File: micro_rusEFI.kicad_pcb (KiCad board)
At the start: 4 copper layers, 80.6 x 93.7 mm, 180 parts, among them J1 USB_B_Micro, J19 Conn_01x06, J2 Conn_02x05_Odd_Even, J7 TC2030, SW1 SW_Push, SW2 SW_Push, SW3 SW_Push, SW4 SW_Push, U1 STM32F427VGT6, U2 LMR14020, U3 molex_48pin_MRE, U35 MCP6004, U36 MCP6004, U4 TJA1051T-3, U46 MCP6004, U5 LM1117-3.3, U6 TJA1051T-3, U8 MCP6004, X1 8MHz 20pF, Y2 32768 Hz

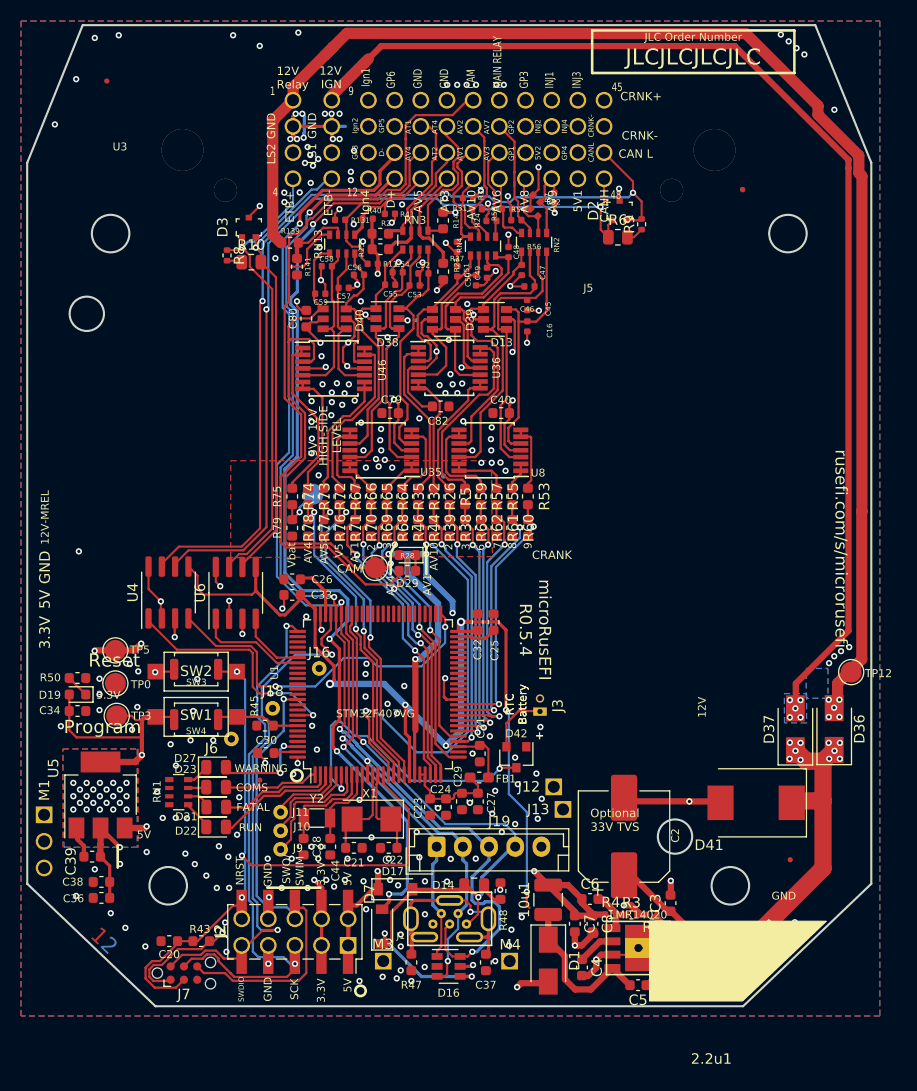
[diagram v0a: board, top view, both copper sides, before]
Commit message: Fixed CAN and 5v pads
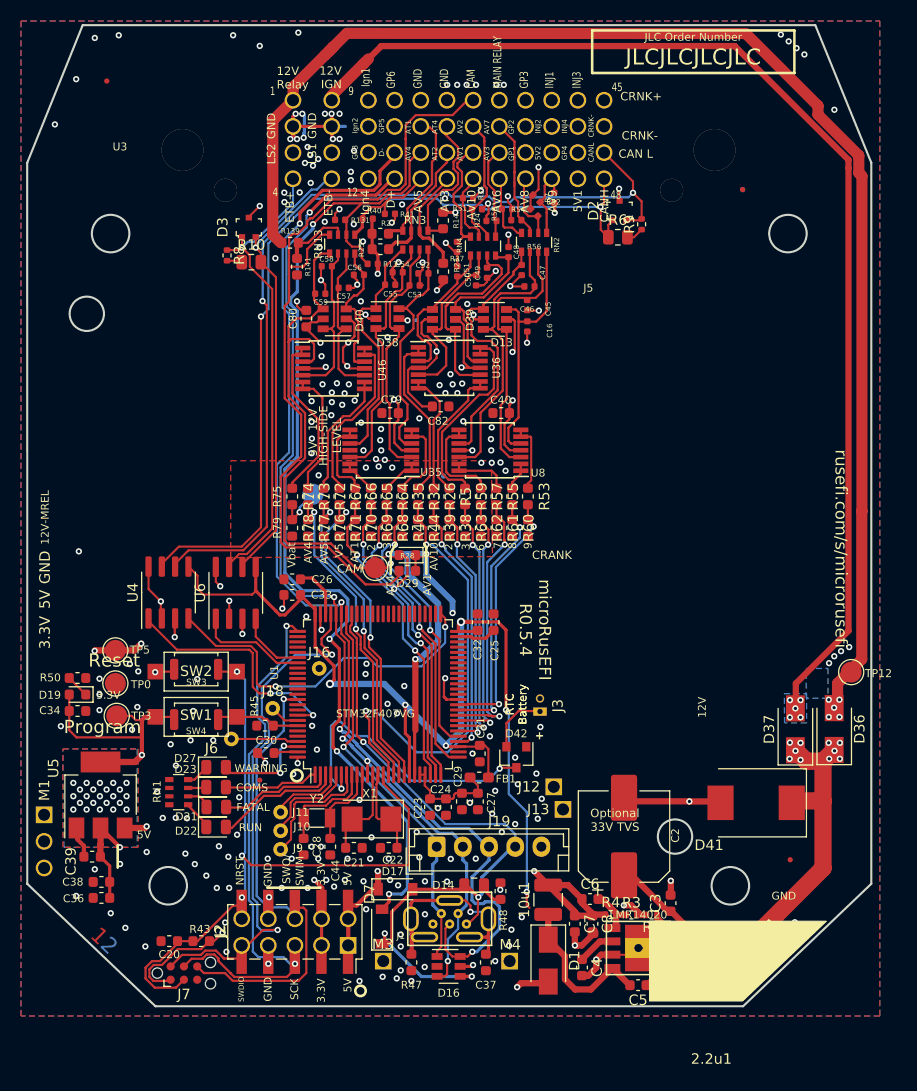
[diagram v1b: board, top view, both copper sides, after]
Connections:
- net /5V renamed 5V
- net /MCU/PB12 renamed /MCU/RXDCAN1
- net /VDD renamed VDD
- D2 pad 1: /CANH -> /CAN Transceiver/CANH1
- D2 pad 2: /CANL -> /CAN Transceiver/CANL1
- D3 pad 1: /CANL2 -> /CAN Transceiver/CANH2
- D3 pad 2: /CANH2 -> /CAN Transceiver/CANL2
- R10 pad 2: /CANH2 -> /CAN Transceiver/CANL2
- R6 pad 1: /CANH -> /CAN Transceiver/CANH1
- R8 pad 1: /CANL2 -> /CAN Transceiver/CANH2
- R9 pad 2: /CANL -> /CAN Transceiver/CANL1
- U3 pad 4: /CANL2 -> unconnected-(U3-Pad4)
- U3 pad 8: /CANH2 -> unconnected-(U3-Pad8)
- U4 pad 6: /CANH -> /CAN Transceiver/CANL1
- U4 pad 7: /CANL -> /CAN Transceiver/CANH1
- U6 pad 6: /CANH2 -> /CAN Transceiver/CANL2
- U6 pad 7: /CANL2 -> /CAN Transceiver/CANH2
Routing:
- net /CANL: track 85.8 -> 0.00 mm, vias 2 -> 0
- net /CAN Transceiver/CANL1: track 0.00 -> 85.1 mm, vias 0 -> 2
- net /CAN Transceiver/CANH1: track 0.00 -> 80.4 mm, vias 0 -> 2
- net /CANH: track 79.4 -> 0.00 mm, vias 2 -> 0
- net /CANL2: track 45.3 -> 0.00 mm, vias 1 -> 0
- net /CAN Transceiver/CANH2: track 0.00 -> 45.3 mm, vias 0 -> 1
- net /CANH2: track 43.8 -> 0.00 mm, vias 1 -> 0
- net /CAN Transceiver/CANL2: track 0.00 -> 43.8 mm, vias 0 -> 1
- net /MCU/PD1: track 0.00 -> 10.6 mm
- net /CAN Transceiver/TXDCAN2: track 10.6 -> 0.00 mm
- net /MCU/PD0: track 0.00 -> 6.53 mm
- net /CAN Transceiver/RXDCAN2: track 6.53 -> 0.00 mm
- net /PE0: track 0.00 -> 6.42 mm
- net /MCU/PB7: track 0.00 -> 2.86 mm

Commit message: Fixing tags
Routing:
- net /ADC/AGND: track 27.0 -> 37.3 mm
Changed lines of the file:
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@@
   (via (at 49.6824 57.4802) (size 0.6) (drill 0.3) (layers "F.Cu" "B.Cu") (net 1))
   (via (at 55 87.2) (size 0.6) (drill 0.3) (layers "F.Cu" "B.Cu") (net 1))
-  (via (at 79.216592 110.522348) (size 0.6) (drill 0.3) (layers "F.Cu" "B.Cu") (net 1))
+  (via (at 78.950449 110.517255) (size 0.6) (drill 0.3) (layers "F.Cu" "B.Cu") (net 1))
   (via (at 44.293286 44.657115) (size 0.6) (drill 0.3) (layers "F.Cu" "B.Cu") (net 1))
   (via (at 83.82 96.52) (size 0.6) (drill 0.3) (layers "F.Cu" "B.Cu") (free) (net 1))
@@
   (segment (start 52.697212 73.403792) (end 52.697212 71.965293) (width 0.2159) (layer "B.Cu") (net 70))
   (segment (start 56.977001 77.683581) (end 52.697212 73.403792) (width 0.2159) (layer "B.Cu") (net 70))
-  (segment (start 51.16464 72.064636) (end 52.100004 73) (width 0.2159) (layer "F.Cu") (net 71))
+  (segment (start 51.461883 72.3465) (end 51.16464 72.049257) (width 0.2159) (layer "F.Cu") (net 71))
   (segment (start 58.472361 92.455841) (end 58.472361 82.945397) (width 0.2159) (layer "F.Cu") (net 71))
   (segment (start 51.9 68.1875) (end 51.9 69.6125) (width 0.2159) (layer "F.Cu") (net 71))
-  (segment (start 51.16464 70.34786) (end 51.16464 72.064636) (width 0.2159) (layer "F.Cu") (net 71))
-  (segment (start 51.9 69.6125) (end 51.16464 70.34786) (width 0.2159) (layer "F.Cu") (net 71))
+  (segment (start 51.16464 72.049257) (end 51.16464 70.34786) (width 0.2159) (layer "F.Cu") (net 71))
   (segment (start 59.0868 93.9596) (end 59.0868 93.07028) (width 0.2159) (layer "F.Cu") (net 71))
   (segment (start 59.0868 93.07028) (end 58.472361 92.455841) (width 0.2159) (layer "F.Cu") (net 71))
+  (segment (start 51.16464 70.34786) (end 51.9 69.6125) (width 0.2159) (layer "F.Cu") (net 71))
   (segment (start 57.632561 82.105597) (end 58.472361 82.945397) (width 0.2159) (layer "F.Cu") (net 71))
   (via (at 57.632561 82.105597) (size 0.6) (drill 0.3) (layers "F.Cu" "B.Cu") (net 71))
-  (via (at 52.100004 73) (size 0.6) (drill 0.3) (layers "F.Cu" "B.Cu") (net 71))
-  (segment (start 52.100004 73.327454) (end 52.100004 73) (width 0.2159) (layer "B.Cu") (net 71))
-  (segment (start 56.462648 80.935684) (end 56.462648 77.690098) (width 0.2159) (layer "B.Cu") (net 71))
-  (segment (start 56.462648 77.690098) (end 52.100004 73.327454) (width 0.2159) (layer "B.Cu") (net 71))
-  (segment (start 57.632561 82.105597) (end 56.462648 80.935684) (width 0.2159) (layer "B.Cu") (net 71))
+  (via (at 51.461883 72.3465) (size 0.6) (drill 0.3) (layers "F.Cu" "B.Cu") (net 71))
+  (segment (start 51.461883 72.689333) (end 56.462648 77.690098) (width 0.2159) (layer "B.Cu") (net 71))
+  (segment (start 51.461883 72.3465) (end 51.461883 72.689333) (width 0.2159) (layer "B.Cu") (net 71))
+  (segment (start 56.462648 77.690098) (end 56.462648 80.935684) (width 0.2159) (layer "B.Cu") (net 71))
+  (segment (start 56.462648 80.935684) (end 57.632561 82.105597) (width 0.2159) (layer "B.Cu") (net 71))
   (segment (start 54.8875 69.6125) (end 54.156957 70.343043) (width 0.2159) (layer "F.Cu") (net 72))
   (segment (start 59.20898 81.62066) (end 58.214436 80.626116) (width 0.2159) (layer "F.Cu") (net 72))
@@
   (segment (start 45.9 66.6125) (end 45.9 66.075) (width 0.2159) (layer "F.Cu") (net 118))
   (segment (start 45.917229 53.920871) (end 45.96168 53.87642) (width 0.2159) (layer "F.Cu") (net 118))
+  (segment (start 52.849135 72.9) (end 55.1 72.9) (width 0.2032) (layer "F.Cu") (net 119))
+  (segment (start 51.9 71.1875) (end 51.9 71.950865) (width 0.2032) (layer "F.Cu") (net 119))
   (segment (start 57.5868 93.9596) (end 57.5868 89.9576) (width 0.3048) (layer "F.Cu") (net 119))
+  (segment (start 51.111196 72.9) (end 55.1 72.9) (width 0.2032) (layer "F.Cu") (net 119))
   (segment (start 66.9 71.1875) (end 66.9 71.37068) (width 0.2159) (layer "F.Cu") (net 119))
+  (segment (start 50.4 72.188804) (end 51.111196 72.9) (width 0.2032) (layer "F.Cu") (net 119))
+  (segment (start 50.4 71.1875) (end 50.4 72.188804) (width 0.2032) (layer "F.Cu") (net 119))
   (segment (start 57.658 82.931) (end 57.658 89.7128) (width 0.6) (layer "F.Cu") (net 119))
+  (segment (start 51.9 71.950865) (end 52.849135 72.9) (width 0.2032) (layer "F.Cu") (net 119))
   (via (at 58.7 72.9) (size 0.6) (drill 0.3) (layers "F.Cu" "B.Cu") (net 119))
   (via (at 55.1 72.9) (size 0.6) (drill 0.3) (layers "F.Cu" "B.Cu") (net 119))

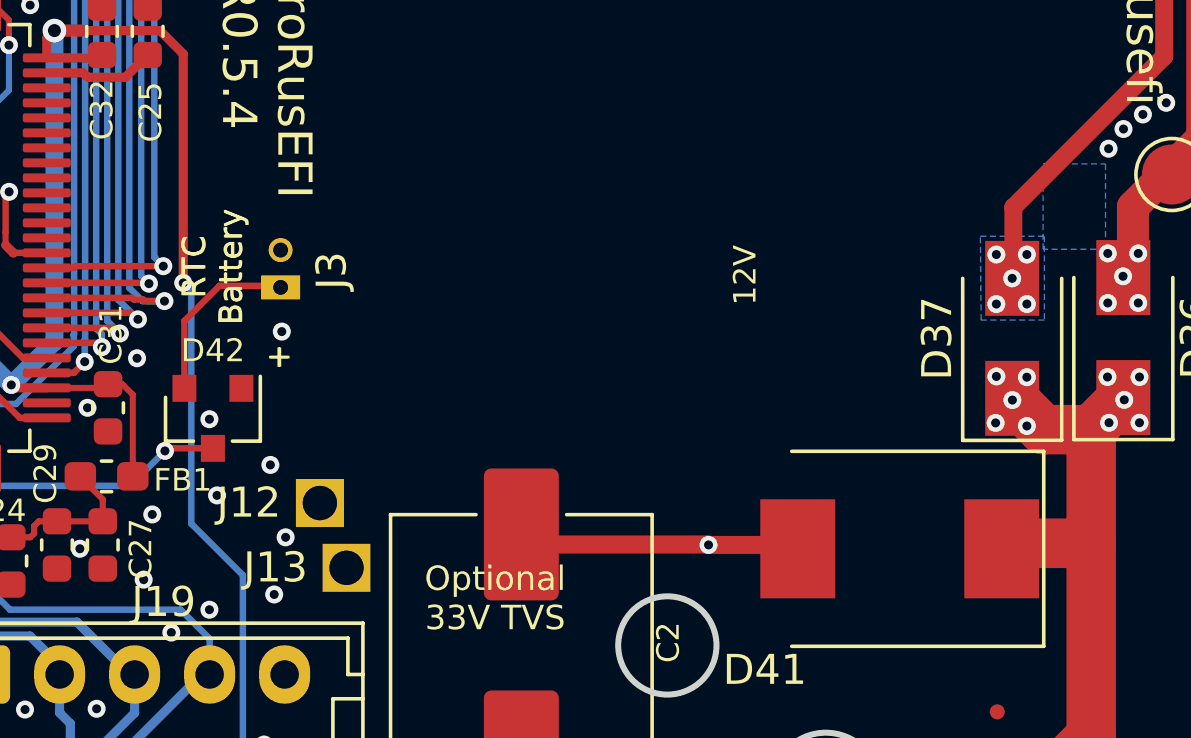
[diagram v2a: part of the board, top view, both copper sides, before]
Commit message: 5v supplies added
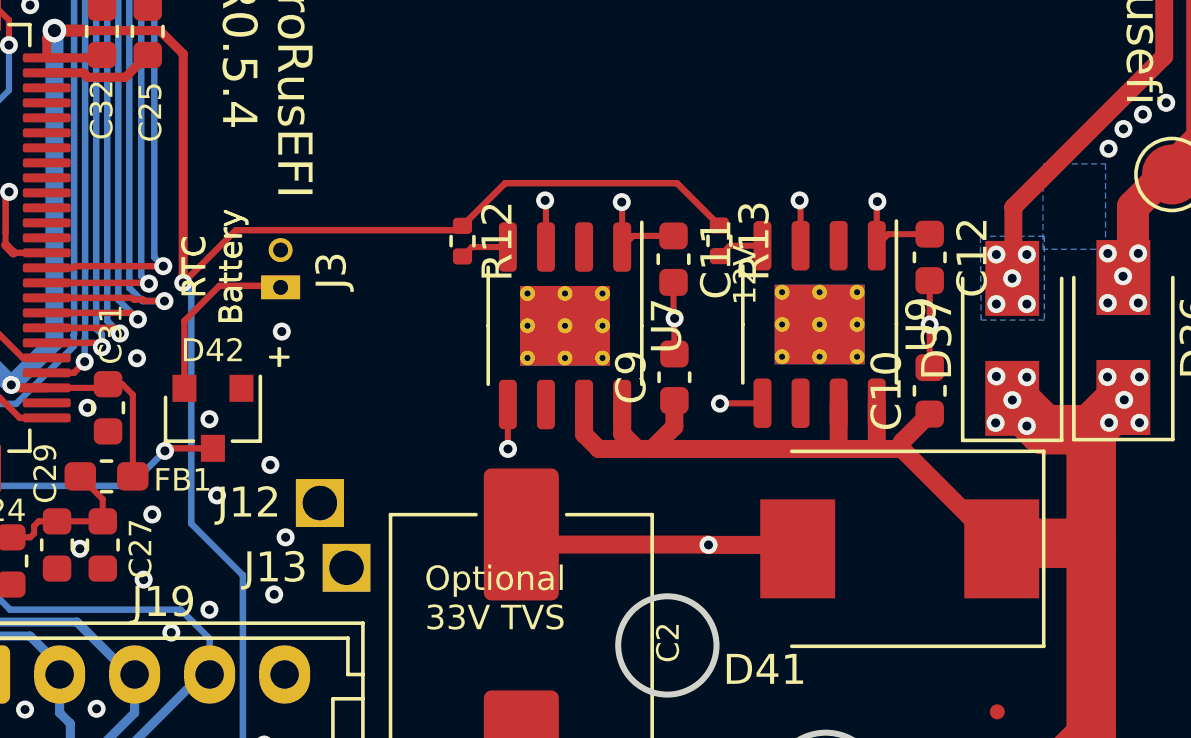
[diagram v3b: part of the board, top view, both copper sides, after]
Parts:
- added C10: 1u, Capacitor_SMD:C_0603_1608Metric, F.Cu at (91.2, 91.4)
- added C11: 1u, Capacitor_SMD:C_0603_1608Metric, F.Cu at (82.7, 87.0)
- added C12: 1u, Capacitor_SMD:C_0603_1608Metric, F.Cu at (91.2, 86.9)
- added C9: 1u, Capacitor_SMD:C_0603_1608Metric, F.Cu at (82.7, 90.9)
- added R12: 10k, Resistor_SMD:R_0402_1005Metric, F.Cu at (75.6, 86.4)
- added R13: 10k, Resistor_SMD:R_0402_1005Metric, F.Cu at (84.2, 86.4)
- added U7: TLS115, Package_SO:Infineon_PG-DSO-8-27_3.9x4.9mm_EP2.65x3mm_ThermalVias, F.Cu at (79.0, 89.2)
- added U9: TLS115, Package_SO:Infineon_PG-DSO-8-27_3.9x4.9mm_EP2.65x3mm_ThermalVias, F.Cu at (87.5, 89.2)
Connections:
- U3 pad 39: /5V2 -> 5V2
- U3 pad 44: /5V1 -> 5V1
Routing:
- net 5V1: track 0.00 -> 64.7 mm, vias 0 -> 1
- net 5V2: track 0.00 -> 61.3 mm, vias 0 -> 1
- net /MCU/RXDCAN1: track 34.3 -> 0.00 mm, vias 2 -> 0
- net /CAN Transceiver/RXDCAN1: track 0.00 -> 34.3 mm, vias 0 -> 2
- net /12V_SAFE: track 34.3 -> 59.6 mm
- net 5V: track 320.5 -> 345.2 mm, vias 20 -> 22
- net VDD: track 214.5 -> 234.4 mm
- net /5V2: track 14.5 -> 0.00 mm
- net /5V1: track 12.6 -> 0.00 mm
- net /MCU/PD1: track 10.6 -> 0.00 mm
- net /CAN Transceiver/TXDCAN2: track 0.00 -> 10.6 mm
- net GND: track 130.0 -> 138.4 mm, vias 238 -> 242
- net Net-(R12-Pad2): track 0.00 -> 1.64 mm
- net Net-(R13-Pad2): track 0.00 -> 1.58 mm

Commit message: Work on 6 axis
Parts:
- added C13: 100nF, Capacitor_SMD:C_0402_1005Metric, F.Cu at (75.2, 90.9)
- added C14: 100nF, Capacitor_SMD:C_0402_1005Metric, F.Cu at (74.6, 88.1)
- added U10: LSM6DS3, Package_LGA:LGA-14_3x2.5mm_P0.5mm_LayoutBorder3x4y, F.Cu at (72.7, 90.4)
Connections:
- net /MCU/PB4 renamed /MCU/SDO
- net /MCU/PB5 renamed /MCU/SDI
- net /MCU/PE15 renamed /MCU/CS
- U1 pad 89: /MCU/PB3 -> SCK
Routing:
- net /MCU/CS: track 0.00 -> 13.0 mm
- net /MCU/PD1: track 0.00 -> 10.6 mm
- net /CAN Transceiver/TXDCAN2: track 10.6 -> 0.00 mm
- net /MCU/PD0: track 6.53 -> 0.00 mm
- net /CAN Transceiver/RXDCAN2: track 0.00 -> 6.53 mm
- net VDD: track 234.4 -> 239.0 mm
- net /MCU/PB3: track 44.4 -> 46.2 mm, vias 1 -> 2
- net Net-(C13-Pad1): track 0.00 -> 1.11 mm
- net CS: vias 0 -> 1
